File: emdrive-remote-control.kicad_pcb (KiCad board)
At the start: 2 copper layers, 107 x 46 mm, 43 parts, among them J1 Raspberry_Pi_2_3, J2 Screw_Terminal_01x06, J3 Conn_01x04, K1 Relay_SPST-NO, Q1 DMN61D8LQ, SW3 SW_Push, SW4 SW_Push, U1 ADS1015IDGS, U2 WS2801SO, U3 AP62150WU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

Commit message: Continues SCH, placed components on PCB
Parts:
- removed SW3, SW4: SW_Push, Button_Switch_THT:SW_PUSH_6mm_H8mm
- added Q2: MMBT3904, Package_TO_SOT_SMD:SOT-23, F.Cu at (149.7, 67.2)
- added R11: 33k, Resistor_SMD:R_0603_1608Metric_Pad0.98x0.95mm_HandSolder, F.Cu at (156.5, 67.4)
- added R12: 33k, Resistor_SMD:R_0603_1608Metric_Pad0.98x0.95mm_HandSolder, F.Cu at (156.5, 65.8)
- added R17: 33k, Resistor_SMD:R_0603_1608Metric_Pad0.98x0.95mm_HandSolder, F.Cu at (149.7, 62.3)
- added R18: 33k, Resistor_SMD:R_0603_1608Metric_Pad0.98x0.95mm_HandSolder, F.Cu at (149.7, 64.1)
- added SW1: SW_Push, Button_Switch_THT:SW_PUSH_6mm_H8mm, F.Cu at (81.8, 53.8)
- added SW2: SW_Push, Button_Switch_THT:SW_PUSH_6mm_H8mm, F.Cu at (82.0, 81.5)
- moved R8 162.1 mm to (85.4, 78.0)
- moved R7 160.3 mm to (85.0, 61.6)
- moved R1 149.3 mm to (93.2, 68.6), turned to 180 degrees
- moved R2 149.2 mm to (93.2, 70.4), turned to 180 degrees
- moved R3 149.1 mm to (93.2, 72.2), turned to 180 degrees
- moved C1 130.8 mm to (109.6, 76.0), turned to 180 degrees
- moved C4 126.1 mm to (123.8, 78.8), turned to 90 degrees
- moved U3 124.9 mm to (129.8, 79.2)
- moved C2 119.9 mm to (126.7, 79.4), turned to -90 degrees
- moved U2 117.9 mm to (109.4, 70.2), turned to 180 degrees
- moved D1 115.3 mm to (142.1, 62.3), turned to 180 degrees
- moved R10 114.8 mm to (130.6, 67.4)
- moved R9 114.8 mm to (130.6, 64.9)
- moved R4 110.6 mm to (133.8, 79.8), turned to 180 degrees
- moved R5 110.4 mm to (133.8, 81.4)
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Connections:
- C10 pad 1: GNDA -> GND
- C11 pad 1: GNDA -> GND
- C12 pad 1: GNDA -> GND
- C6 pad 1: GNDA -> GND
- J1 pad 1: Net-(J1-3V3-Pad1) -> +3.3V
- J1 pad 14: Net-(J1-GND-Pad14) -> GND
- J1 pad 15: unconnected-(J1-GPIO22-Pad15) -> /IN_LED_R
- J1 pad 16: unconnected-(J1-GPIO23-Pad16) -> /IN_LED_G
- J1 pad 17: Net-(J1-3V3-Pad1) -> +3.3V
- J1 pad 18: unconnected-(J1-GPIO24-Pad18) -> /IN_LED_Y
- J1 pad 19: unconnected-(J1-MOSI0/GPIO10-Pad19) -> /SPI_MOSI
- J1 pad 2: Net-(J1-5V-Pad2) -> +5V
- J1 pad 20: Net-(J1-GND-Pad14) -> GND
- J1 pad 23: unconnected-(J1-SCLK0/GPIO11-Pad23) -> /SPI_SCLK
- J1 pad 25: Net-(J1-GND-Pad14) -> GND
- J1 pad 26: unconnected-(J1-~{CE1}/GPIO7-Pad26) -> /WDT_EN
- J1 pad 29: unconnected-(J1-GCLK1/GPIO5-Pad29) -> /BTN_2
- J1 pad 3: unconnected-(J1-SDA/GPIO2-Pad3) -> /I2C_SDA
- J1 pad 30: Net-(J1-GND-Pad14) -> GND
- J1 pad 31: unconnected-(J1-GCLK2/GPIO6-Pad31) -> /DRIVE_PS_EN
- J1 pad 34: Net-(J1-GND-Pad14) -> GND
- J1 pad 39: Net-(J1-GND-Pad14) -> GND
- J1 pad 4: Net-(J1-5V-Pad2) -> +5V
- J1 pad 5: unconnected-(J1-SCL/GPIO3-Pad5) -> /I2C_SCL
- J1 pad 6: Net-(J1-GND-Pad14) -> GND
- J1 pad 7: unconnected-(J1-GCLK0/GPIO4-Pad7) -> /BTN_1
- J1 pad 9: Net-(J1-GND-Pad14) -> GND
- J2 pad 1: unconnected-(J2-Pin_1-Pad1) -> +12V
- J2 pad 2: unconnected-(J2-Pin_2-Pad2) -> GND
- J2 pad 3: unconnected-(J2-Pin_3-Pad3) -> Net-(J2-Pin_3)
- J2 pad 4: unconnected-(J2-Pin_4-Pad4) -> GND
- J2 pad 5: unconnected-(J2-Pin_5-Pad5) -> /WDT_P1
- J2 pad 6: unconnected-(J2-Pin_6-Pad6) -> /WDT_P2
- K1 pad 13: +12V -> /WDT_P2
- K1 pad 14: +12L -> /WDT_P1
- Q1 pad 1: Net-(Q1-G) -> /WDT_EN
- R10 pad 2: Net-(U1-SDA) -> /I2C_SDA
- R14 pad 2: unconnected-(R14-Pad2) -> /I_SENSE
- R16 pad 2: Net-(J4-Pin_4) -> GND
- R6 pad 2: Net-(Q1-G) -> /WDT_EN
- R7 pad 1: Net-(R7-Pad1) -> /BTN_1
- R8 pad 1: Net-(R8-Pad1) -> /BTN_2
- R9 pad 2: Net-(U1-SCL) -> /I2C_SCL
- U1 pad 1: GNDA -> GND
- U1 pad 10: Net-(U1-SCL) -> /I2C_SCL
- U1 pad 3: GNDA -> GND
- U1 pad 9: Net-(U1-SDA) -> /I2C_SDA
- U2 pad 1: unconnected-(U2-CKI-Pad1) -> /SPI_SCLK
- U2 pad 2: unconnected-(U2-SDI-Pad2) -> /SPI_MOSI
- U4 pad 3: Net-(U1-SCL) -> /I2C_SCL
- U4 pad 4: Net-(U1-SDA) -> /I2C_SDA
- U5 pad 3: unconnected-(U5-Y1-Pad3) -> /IN_LED_R
- U5 pad 6: unconnected-(U5-Y2-Pad6) -> /IN_LED_G
- U5 pad 8: unconnected-(U5-Y3-Pad8) -> /IN_LED_Y
- U6 pad 4: GNDA -> GND
- U7 pad 1: Net-(U7-OUT-Pad1) -> Net-(J2-Pin_3)
- U7 pad 2: unconnected-(U7-IN-Pad2) -> Net-(U7-IN)
- U7 pad 3: unconnected-(U7-Vbb-Pad3) -> +12V
- U7 pad 4: unconnected-(U7-IS-Pad4) -> /I_SENSE
- U7 pad 5: Net-(U7-OUT-Pad1) -> Net-(J2-Pin_3)

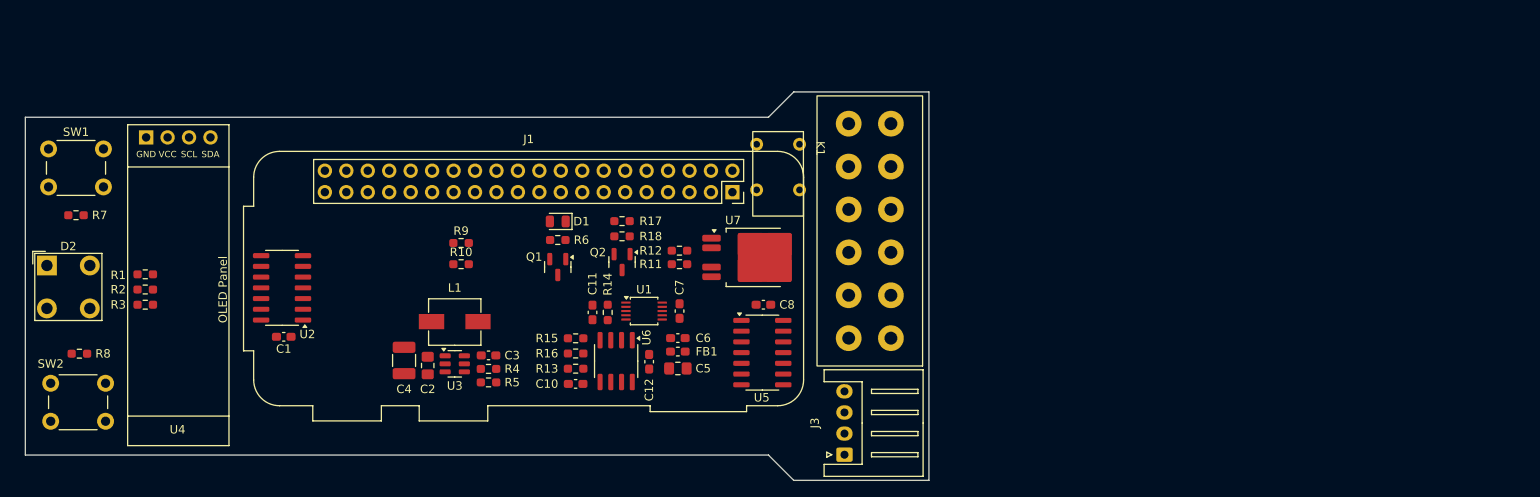
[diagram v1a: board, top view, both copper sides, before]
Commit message: Initial Routing. Minor modifications to .sch. SCH verified.
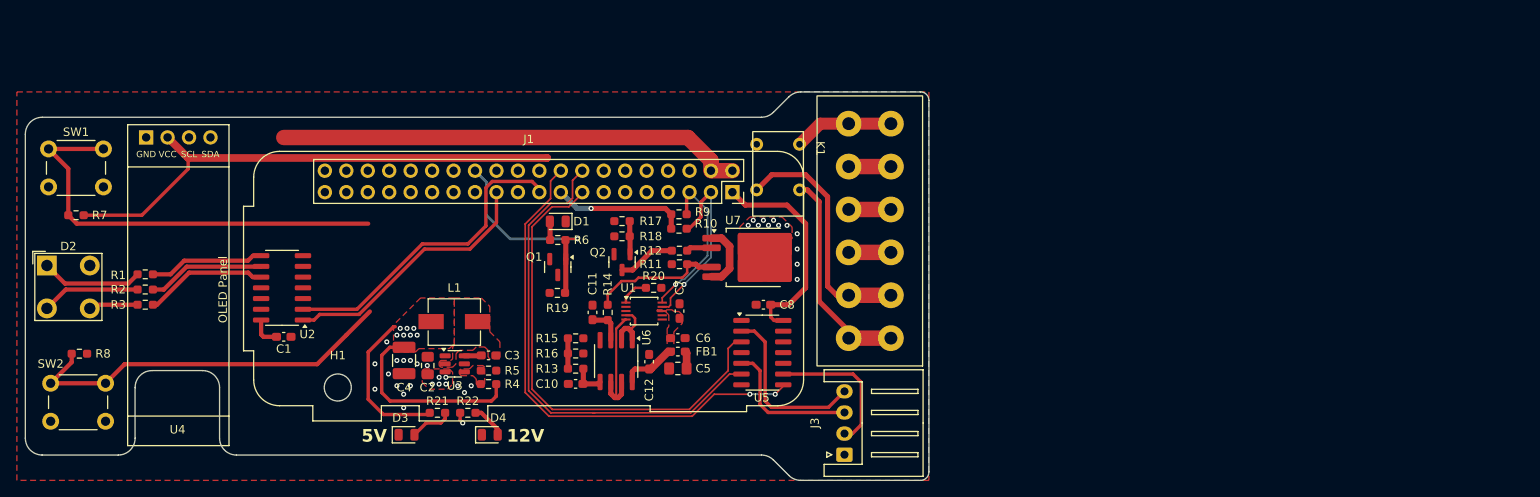
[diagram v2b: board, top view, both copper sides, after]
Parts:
- added D3: LED, LED_SMD:LED_0805_2012Metric, F.Cu at (124.1, 87.6)
- added D4: LED, LED_SMD:LED_0805_2012Metric, F.Cu at (134.0, 87.6)
- added H1: MountingHole, MountingHole:MountingHole_3.2mm_M3_DIN965, F.Cu at (116.0, 82.0)
- added R19: 0R, Resistor_SMD:R_0603_1608Metric_Pad0.98x0.95mm_HandSolder, F.Cu at (142.0, 70.8)
- added R20: 0R, Resistor_SMD:R_0603_1608Metric_Pad0.98x0.95mm_HandSolder, F.Cu at (153.4, 70.2)
- added R21: 220R, Resistor_SMD:R_0603_1608Metric_Pad0.98x0.95mm_HandSolder, F.Cu at (127.8, 85.0)
- added R22: 1k, Resistor_SMD:R_0603_1608Metric_Pad0.98x0.95mm_HandSolder, F.Cu at (131.4, 85.0)
- moved R10 26.1 mm to (156.4, 63.2)
- moved R9 26.0 mm to (156.4, 61.5)
- moved R4 1.80 mm to (133.8, 81.6)
- moved R5 1.40 mm to (133.8, 80.0)
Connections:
- U1 pad 1: GND -> Net-(U1-ADDR)
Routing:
- net +3.3V: track 0.00 -> 103.7 mm, vias 0 -> 1
- net +5V: track 0.00 -> 102.4 mm, vias 0 -> 7
- net /IN_LED_Y: track 0.00 -> 61.4 mm, vias 0 -> 2
- net /IN_LED_G: track 0.00 -> 58.2 mm
- net /IN_LED_R: track 0.00 -> 57.6 mm
- net /BTN_1: track 0.00 -> 51.2 mm
- net /BTN_2: track 0.00 -> 45.9 mm
- net /SPI_MOSI: track 0.00 -> 37.7 mm
- net /SPI_SCLK: track 0.00 -> 31.3 mm
- net /WDT_P1: track 0.00 -> 28.8 mm
- net /WDT_EN: track 0.00 -> 25.6 mm, vias 0 -> 1
- net /WDT_P2: track 0.00 -> 25.5 mm
- net /I2C_SDA: track 0.00 -> 22.1 mm, vias 0 -> 1
- net Net-(J3-Pin_4): track 0.00 -> 20.8 mm
- net /I2C_SCL: track 0.00 -> 19.2 mm, vias 0 -> 1
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- added copper zone on F.Cu, net +12V
- added copper zone on In2.Cu, net +12V
- added copper zone on F.Cu, net +5V
- added copper zone on F.Cu, net +5VA
- added copper zone on F.Cu, net GND
- added copper zone on F.Cu, net Net-(U3-FB)
- added copper zone on F.Cu, net Net-(U3-SW)
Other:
- outline, holes or cut-outs redrawn
- copper layers 2 -> 4
- board text added: "12V"
- board text added: "5V"

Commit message: Moved around modules on the PCB. Minor fixes in SCH.
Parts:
- moved R10 60.4 mm to (96.0, 60.9), turned to 90 degrees
- moved R9 58.4 mm to (98.0, 60.9), turned to 90 degrees
- moved C4 33.2 mm to (157.0, 76.4), turned to 180 degrees
- moved C2 31.5 mm to (157.6, 73.6), turned to 0 degrees
- moved R4 30.0 mm to (159.8, 66.4), turned to -90 degrees
- moved U3 28.9 mm to (157.4, 70.4), turned to 90 degrees
- moved R5 27.9 mm to (158.2, 66.4), turned to 90 degrees
- moved D1 25.9 mm to (151.5, 86.5), turned to 90 degrees
- moved C3 25.4 mm to (156.4, 66.4), turned to 90 degrees
- moved R6 23.1 mm to (149.3, 86.5), turned to -90 degrees
- moved L1 22.9 mm to (152.4, 70.5), turned to -90 degrees
- moved R17 19.6 mm to (147.6, 81.8), turned to 90 degrees
- moved Q1 19.1 mm to (146.1, 86.5), turned to 180 degrees
- moved C5 18.5 mm to (137.8, 78.8), turned to -90 degrees
- moved K1 18.3 mm to (167.0, 75.0)
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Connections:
- C7 pad 1: GNDA -> GND
- J1 pad 15: /IN_LED_R -> /IN_LED_G
- J1 pad 16: /IN_LED_G -> /IN_LED_Y
- J1 pad 18: /IN_LED_Y -> /IN_LED_R
- J1 pad 29: /BTN_2 -> unconnected-(J1-GCLK1/GPIO5-Pad29)
- J1 pad 33: unconnected-(J1-PWM1/GPIO13-Pad33) -> /BTN_2
- J1 pad 36: unconnected-(J1-GPIO16-Pad36) -> /BTN_1
- J1 pad 38: unconnected-(J1-GPIO20/MOSI1-Pad38) -> /SPI_MOSI
- J1 pad 40: unconnected-(J1-GPIO21/SCLK1-Pad40) -> /SPI_SCLK
- J1 pad 7: /BTN_1 -> unconnected-(J1-GCLK0/GPIO4-Pad7)
- J2 pad 3: Net-(J2-Pin_3) -> +12L
- U7 pad 1: Net-(J2-Pin_3) -> +12L
- U7 pad 5: Net-(J2-Pin_3) -> +12L
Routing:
- net +12V: track 13.2 -> 132.9 mm, vias 14 -> 7
- net +5V: track 102.4 -> 33.1 mm, vias 7 -> 10
- net /I2C_SDA: track 22.1 -> 76.6 mm, vias 1 -> 0
- net /I2C_SCL: track 19.2 -> 71.1 mm, vias 1 -> 0
- net /DRIVE_PS_EN: track 0.00 -> 38.4 mm
- net Net-(Q1-D): track 0.00 -> 28.9 mm
- net +12L: track 0.00 -> 28.6 mm
- net +3.3V: track 103.7 -> 81.7 mm
- net /WDT_EN: track 25.6 -> 46.8 mm, vias 1 -> 2
- net Net-(U7-IN): track 3.03 -> 22.9 mm
- net /SPI_MOSI: track 37.7 -> 19.1 mm
- net /IN_LED_Y: track 61.4 -> 45.2 mm, vias 2 -> 1
- net /BTN_2: track 45.9 -> 59.9 mm
- net /I_SENSE: track 15.7 -> 28.6 mm, vias 0 -> 2
- net Net-(J2-Pin_3): track 12.7 -> 0.00 mm
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- added copper zone on F.Cu, net +12L
- added copper zone on In2.Cu, net +5V
- added copper zone on In1.Cu, net GND
- removed copper zone on In2.Cu, net +12V
